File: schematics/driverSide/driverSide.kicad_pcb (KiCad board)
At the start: 2 copper layers, 46 parts, among them J1 Conn_01x20, J10 Conn_01x20, J11 Conn_01x20, J12 Conn_01x20, J13 Conn_01x20, J14 Conn_01x20, J15 Conn_01x20, J16 Conn_01x20, J17 Conn_01x20, J18 Conn_01x20, J19 PINHD_1x8_Male, J2 OLEDdisp, J20 PINHD_1x8_Male, J21 Conn_01x02, J22 Screw_Terminal_01x02, J3 Rotencoder, J4 Conn_01x20, J5 Conn_01x20, J6 Conn_01x20, J7 Conn_01x20, J8 Conn_01x20, J9 Conn_01x20, SW1 Push_Button, U1 PC817, U2 4046, U3 UCC37322, U4 UCC37322

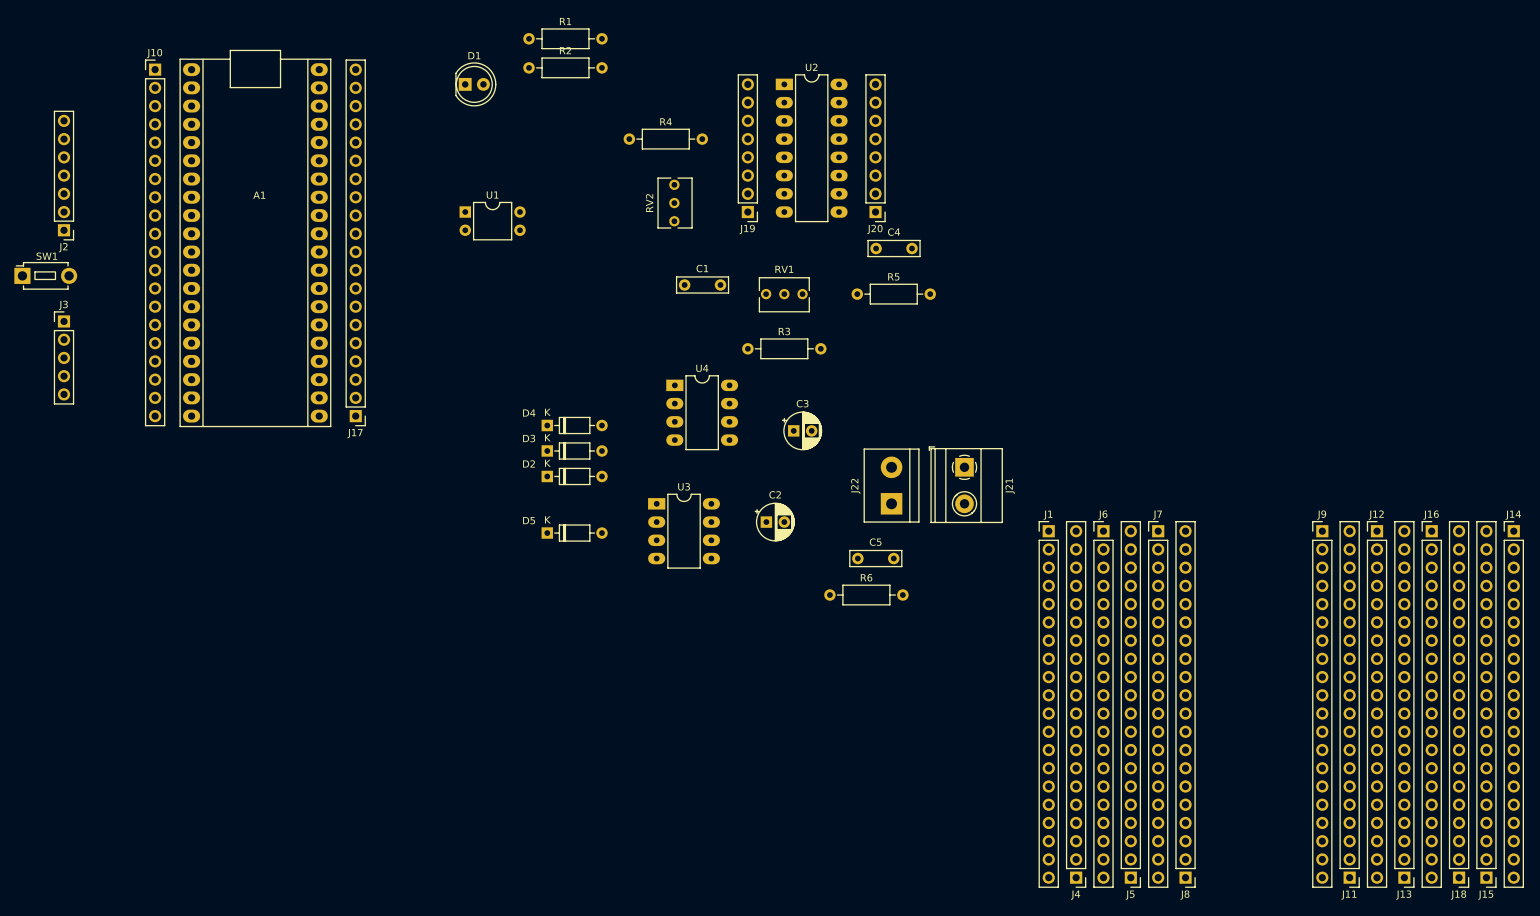
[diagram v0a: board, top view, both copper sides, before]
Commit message: first version driver board completed
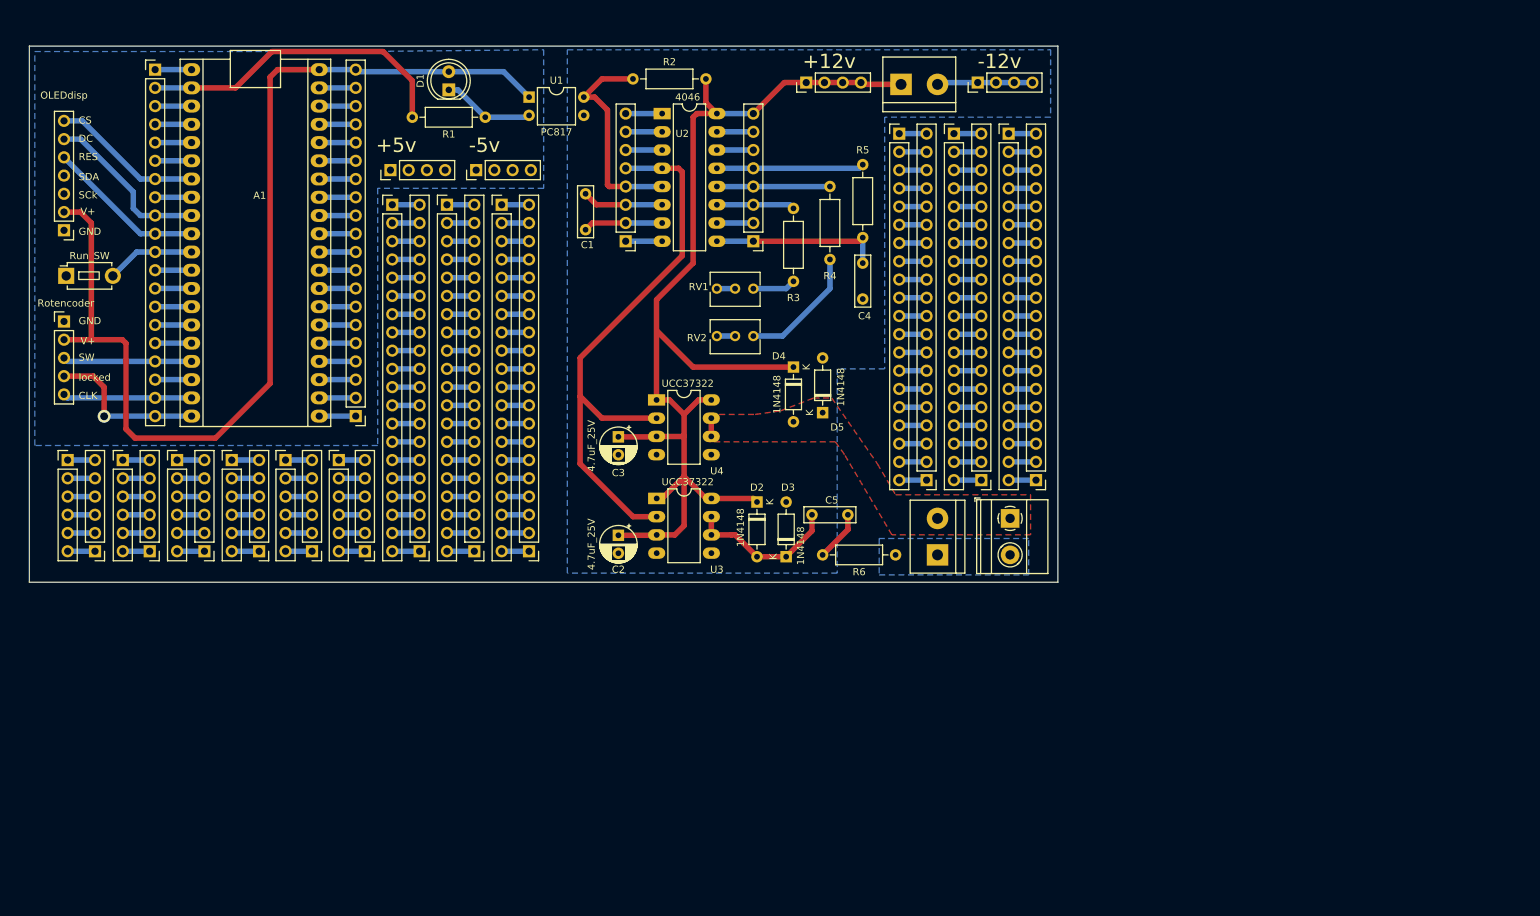
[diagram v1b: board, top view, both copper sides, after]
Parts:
- removed the J14 at (247.7, 105.4)
- removed the J15 at (243.8, 153.7)
- added J17: PINHD_1x6_Male, Connector_PinHeader_2.54mm:PinHeader_1x06_P2.54mm_Vertical, F.Cu at (53.9, 95.5)
- added J18: PINHD_1x6_Male, Connector_PinHeader_2.54mm:PinHeader_1x06_P2.54mm_Vertical, F.Cu at (61.5, 95.5)
- added J19: PINHD_1x6_Male, Connector_PinHeader_2.54mm:PinHeader_1x06_P2.54mm_Vertical, F.Cu at (57.7, 108.2)
- added J20: PINHD_1x6_Male, Connector_PinHeader_2.54mm:PinHeader_1x06_P2.54mm_Vertical, F.Cu at (65.3, 108.2)
- added J21: PINHD_1x6_Male, Connector_PinHeader_2.54mm:PinHeader_1x06_P2.54mm_Vertical, F.Cu at (76.6, 95.5)
- added J22: PINHD_1x6_Male, Connector_PinHeader_2.54mm:PinHeader_1x06_P2.54mm_Vertical, F.Cu at (69.1, 95.5)
- added J23: PINHD_1x6_Male, Connector_PinHeader_2.54mm:PinHeader_1x06_P2.54mm_Vertical, F.Cu at (80.3, 108.2)
- added J24: PINHD_1x6_Male, Connector_PinHeader_2.54mm:PinHeader_1x06_P2.54mm_Vertical, F.Cu at (72.9, 108.2)
- added J25: PINHD_1x6_Male, Connector_PinHeader_2.54mm:PinHeader_1x06_P2.54mm_Vertical, F.Cu at (84.0, 95.5)
- added J27: PINHD_1x6_Male, Connector_PinHeader_2.54mm:PinHeader_1x06_P2.54mm_Vertical, F.Cu at (87.6, 108.2)
- added J31: PINHD_1x6_Male, Connector_PinHeader_2.54mm:PinHeader_1x06_P2.54mm_Vertical, F.Cu at (46.2, 95.5)
- added J32: PINHD_1x6_Male, Connector_PinHeader_2.54mm:PinHeader_1x06_P2.54mm_Vertical, F.Cu at (50.0, 108.2)
- added J33: PINHD_1x4_Male, Connector_PinHeader_2.54mm:PinHeader_1x04_P2.54mm_Vertical, F.Cu at (91.2, 55.1)
- added J34: PINHD_1x4_Male, Connector_PinHeader_2.54mm:PinHeader_1x04_P2.54mm_Vertical, F.Cu at (103.1, 55.1)
- added J35: PINHD_1x4_Male, Connector_PinHeader_2.54mm:PinHeader_1x04_P2.54mm_Vertical, F.Cu at (173.0, 42.9)
- added J36: PINHD_1x4_Male, Connector_PinHeader_2.54mm:PinHeader_1x04_P2.54mm_Vertical, F.Cu at (149.1, 42.9)
- added J37: Screw_Terminal_01x02, TerminalBlock:TerminalBlock_bornier-2_P5.08mm, F.Cu at (162.3, 43.2)
- SW1: value Push_Button -> Run_SW
- moved J8 102.1 mm to (110.5, 108.2)
- moved J1 102.1 mm to (91.4, 59.9)
- moved J4 102.1 mm to (95.2, 108.2)
- moved J5 102.1 mm to (102.9, 108.2)
- moved J6 102.1 mm to (99.1, 59.9)
- moved J7 102.1 mm to (106.7, 59.9)
- moved J11 80.9 mm to (165.9, 98.3)
- moved J12 80.9 mm to (169.7, 50.0)
- moved J13 80.9 mm to (173.5, 98.3)
- moved J14 80.9 mm to (177.3, 50.0)
- moved J15 80.9 mm to (181.1, 98.3)
- moved J9 80.9 mm to (162.1, 50.0)
- moved D5 41.9 mm to (151.4, 88.9), turned to 90 degrees
- moved D3 36.4 mm to (146.3, 109.0), turned to 90 degrees
- moved D4 35.2 mm to (147.3, 82.5), turned to -90 degrees
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- renumbered J16 to J14, J18 to J15, J17 to J16, J19 to J26, J20 to J28, J21 to J29, J22 to J30
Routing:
- net +12V: track 0.00 -> 159.5 mm
- net +5V: track 0.00 -> 146.0 mm
- net Net-(U2-FOUT): track 0.00 -> 80.3 mm
- net Net-(A1-GP1): track 0.00 -> 44.7 mm
- net GND: track 0.00 -> 40.6 mm
- net Net-(U2-Inh): track 0.00 -> 30.1 mm
- net Net-(U2-VCOin): track 0.00 -> 24.1 mm
- net Net-(A1-GP6): track 0.00 -> 23.5 mm
- net GNDD: track 0.00 -> 23.5 mm
- net Net-(A1-GP15): track 0.00 -> 22.5 mm, vias 0 -> 1
- net Net-(A1-GP7): track 0.00 -> 22.2 mm
- net Net-(D2-A): track 0.00 -> 21.6 mm
- net Net-(A1-GP5): track 0.00 -> 21.1 mm
- net Net-(U2-PC2): track 0.00 -> 20.5 mm
- net Net-(A1-GP14): track 0.00 -> 18.0 mm
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- added copper zone on B.Cu, net GND
- added copper zone on B.Cu, net GNDD
- added copper zone on F.Cu, net Net-(D4-A)
- added copper zone on B.Cu, net Net-(J29-Pin_2)
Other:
- board outline added: 143.3 x 74.7 mm
- board text added: "+12v"
- board text added: "+5v"
- board text added: "-12v"
- board text added: "-5v"
- board text added: "CLK"
- board text added: "CS"
- board text added: "DC"
- board text added: "GND"
- board text added: "RES"
- board text added: "SCk"
- board text added: "SDA"
- board text added: "SW"
- board text added: "V+"
- board text added: "locked"
